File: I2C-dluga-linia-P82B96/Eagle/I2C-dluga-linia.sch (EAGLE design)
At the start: 7 parts

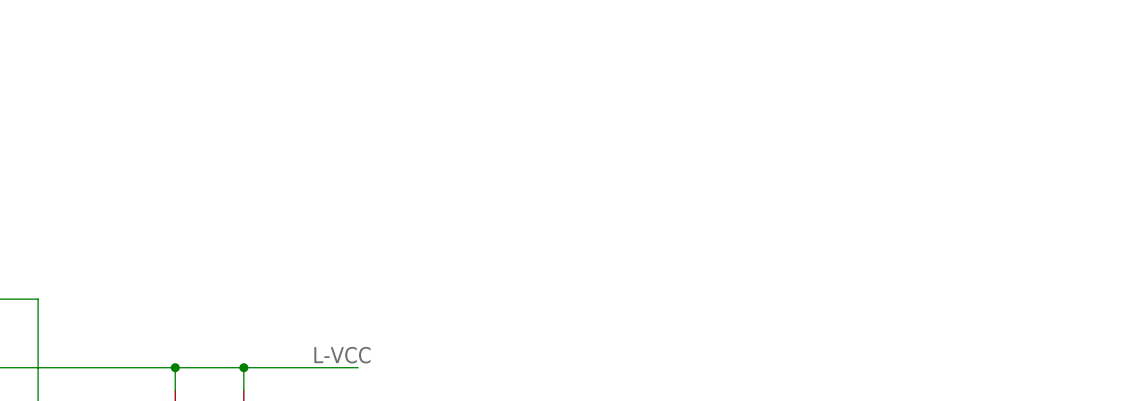
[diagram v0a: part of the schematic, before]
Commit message: złącza do układów
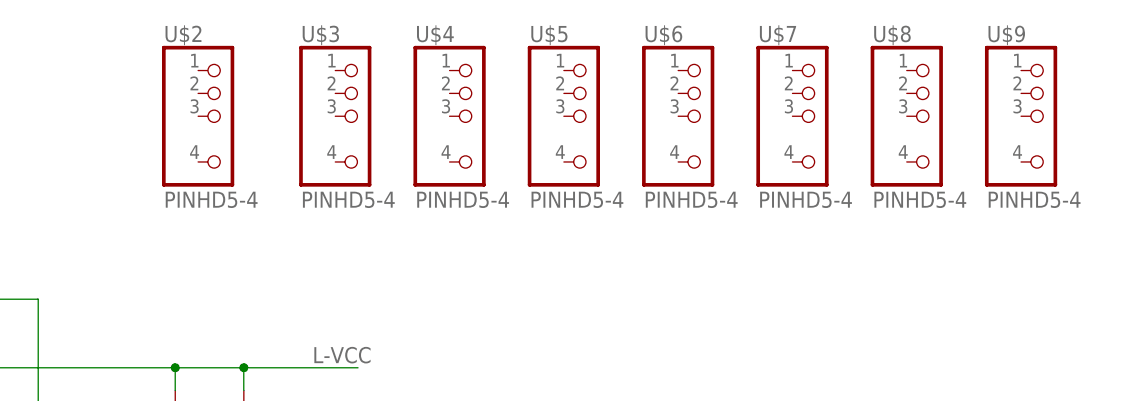
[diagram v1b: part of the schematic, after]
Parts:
- added U$2, U$3, U$4, U$5, U$6, U$7, U$8, U$9: PINHD5-4, RD:PINHD5-4
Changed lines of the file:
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@@
 <?xml version="1.0" encoding="utf-8"?>
 <!DOCTYPE eagle SYSTEM "eagle.dtd">
-<eagle version="7.3.0">
+<eagle version="6.4">
 <drawing>
 <settings>
@@
 <part name="GND2" library="supply1" deviceset="GND" device=""/>
 <part name="GND3" library="supply1" deviceset="GND" device=""/>
+<part name="U$2" library="RD" deviceset="PINHD5-4" device=""/>
+<part name="U$3" library="RD" deviceset="PINHD5-4" device=""/>
+<part name="U$4" library="RD" deviceset="PINHD5-4" device=""/>
+<part name="U$5" library="RD" deviceset="PINHD5-4" device=""/>
+<part name="U$6" library="RD" deviceset="PINHD5-4" device=""/>
+<part name="U$7" library="RD" deviceset="PINHD5-4" device=""/>
+<part name="U$8" library="RD" deviceset="PINHD5-4" device=""/>
+<part name="U$9" library="RD" deviceset="PINHD5-4" device=""/>
 </parts>
 <sheets>
@@
 <instance part="GND2" gate="1" x="68.58" y="33.02"/>
 <instance part="GND3" gate="1" x="12.7" y="33.02"/>
+<instance part="U$2" gate="G$1" x="66.04" y="101.6"/>
+<instance part="U$3" gate="G$1" x="81.28" y="101.6"/>
+<instance part="U$4" gate="G$1" x="93.98" y="101.6"/>
+<instance part="U$5" gate="G$1" x="106.68" y="101.6"/>
+<instance part="U$6" gate="G$1" x="119.38" y="101.6"/>
+<instance part="U$7" gate="G$1" x="132.08" y="101.6"/>
+<instance part="U$8" gate="G$1" x="144.78" y="101.6"/>
+<instance part="U$9" gate="G$1" x="157.48" y="101.6"/>
 </instances>
 <busses>

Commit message: Podłączone złącza
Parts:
- removed U$2, U$3, U$4, U$5, U$6, U$7, U$8, U$9: PINHD5-4, RD:PINHD5-4
- added X1, X2: 22-23-2051, con-molex:22-23-2051
- added X3, X4, X5, X6: 22-23-2041, con-molex:22-23-2041
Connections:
- net GND: now also X1-4.S, X2-4.S, X3-3.S, X4-3.S, X5-3.S, X6-3.S
- net L-SCL: now also X1-3.S, X2-3.S
- net L-SDA: now also X1-5.S, X2-5.S
- net L-VCC: now also X1-2.S, X2-2.S
- net SCL: now also X3-2.S, X4-2.S, X5-2.S, X6-2.S
- net SDA: now also X3-4.S, X4-4.S, X5-4.S, X6-4.S
- net VCC: now also X1-1.S, X2-1.S, X3-1.S, X4-1.S, X5-1.S, X6-1.S
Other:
- moved on the sheet: D1, D2, R1, R2, R3, R4, U$1

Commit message: PCB
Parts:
- added C1, C2: 22p, rcl:C-EUC1206
- added C3: (no value), rcl:CPOL-EUE5-10.5
- added C4: (no value), rcl:CPOL-EUE3.5-8
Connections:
- net GND: now also C1.2, C2.2, C3.-, C4.-, X1-5.S, X2-5.S, X3-4.S, X4-4.S, X5-4.S, X6-4.S; no longer X1-4.S, X2-4.S, X3-3.S, X4-3.S, X5-3.S, X6-3.S
- net L-SDA: now also X1-4.S, X2-4.S; no longer X1-5.S, X2-5.S
- net L-VCC: now also C3.+
- net SCL: now also C2.1
- net SDA: now also C1.1, X3-3.S, X4-3.S, X5-3.S, X6-3.S; no longer X3-4.S, X4-4.S, X5-4.S, X6-4.S
- net VCC: now also C4.+
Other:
- moved on the sheet: D1, D2, R1, R2, R3, R4, X1-1, X1-2, X1-3, X1-4, X1-5, X2-1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

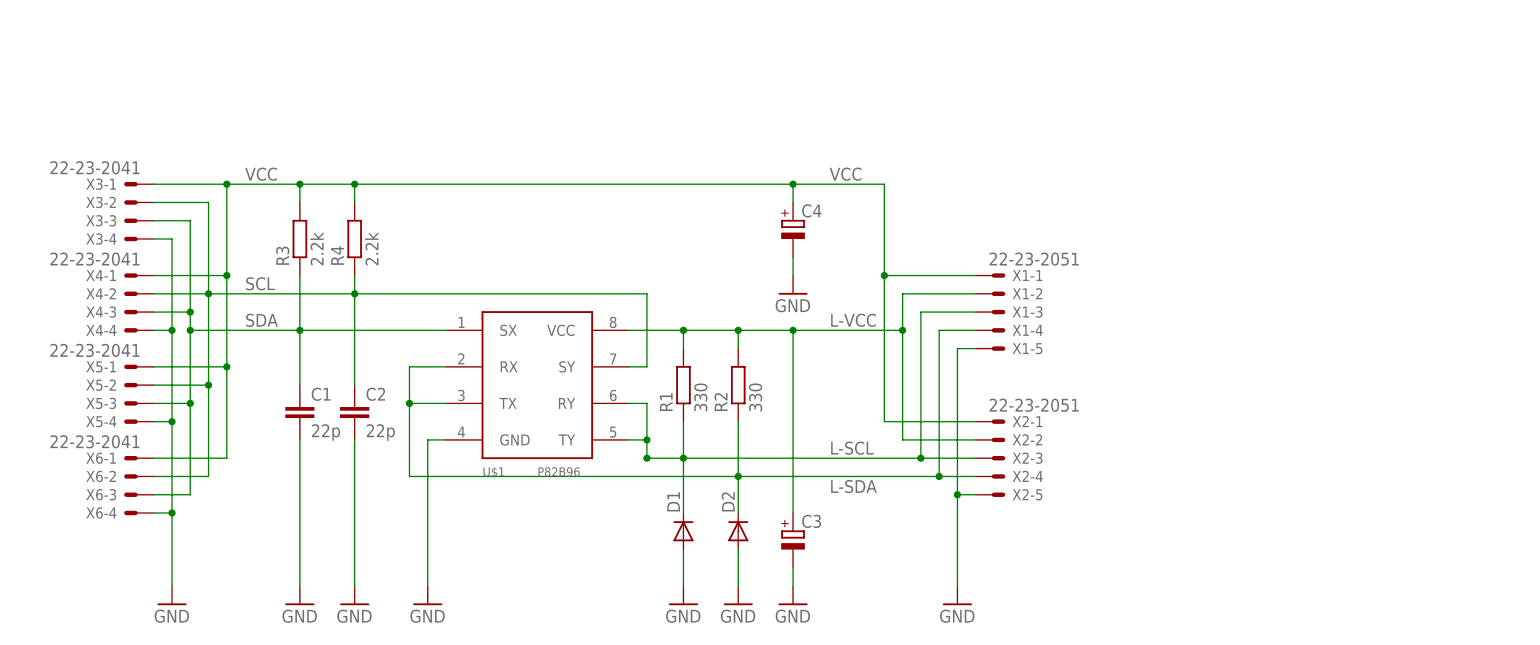
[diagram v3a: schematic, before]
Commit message: Dodatkowe gniazdo zasilania układów
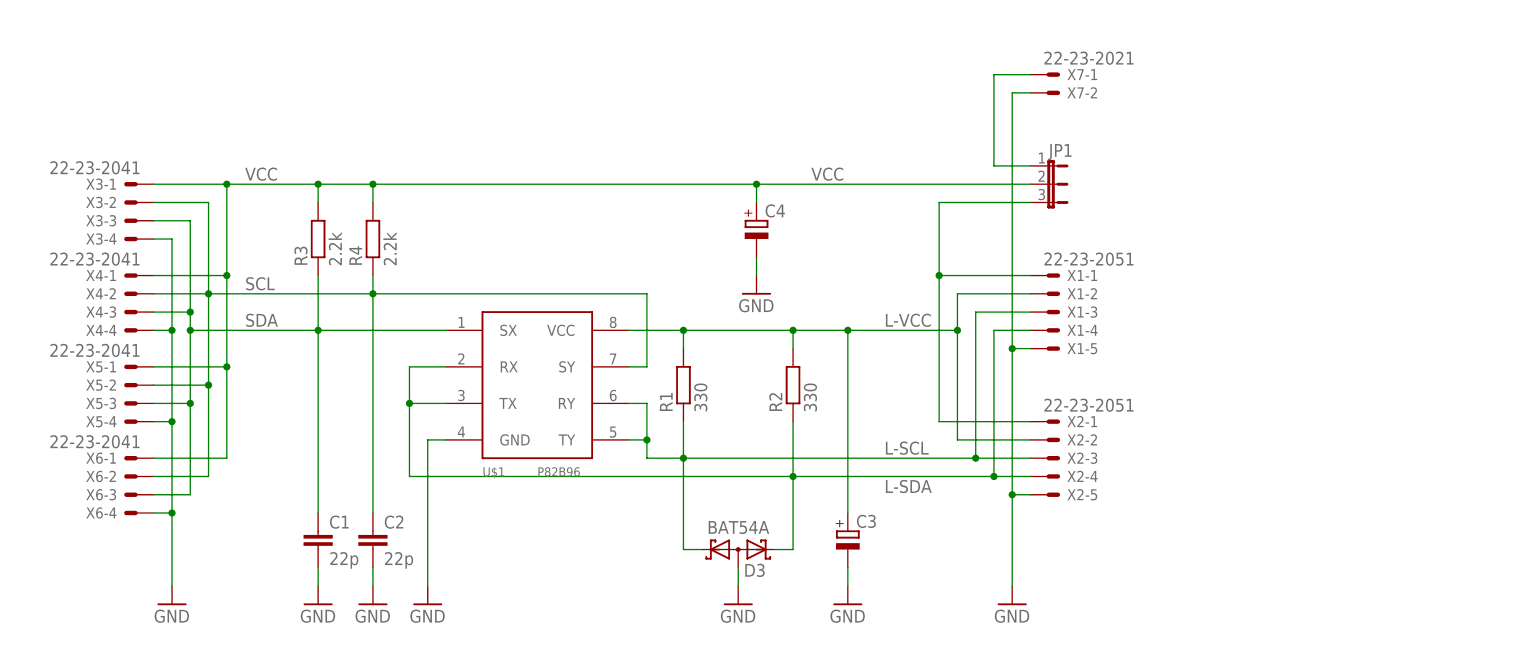
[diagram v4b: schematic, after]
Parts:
- removed D1, D2: (no value), diode:DIODE-MELF-MLL41
- added D3: BAT54A, diode:BAT54A
- added JP1: (no value), jumper:JP2E
- added X7: 22-23-2021, con-molex:22-23-2021
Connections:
- new net N$1: JP1.3, X1-1.S, X2-1.S
- new net N$2: JP1.1, X7-1.S
- net GND: now also D3.AA, X7-2.S; no longer D1.A, D2.A
- net L-SCL: now also D3.K1; no longer D1.C
- net L-SDA: now also D3.K2; no longer D2.C
- net VCC: now also JP1.2; no longer X1-1.S, X2-1.S
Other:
- moved on the sheet: C1, C2, C3, C4, R2, R3, R4, X1-1, X1-2, X1-3, X1-4, X1-5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
